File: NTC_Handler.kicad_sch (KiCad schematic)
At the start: 16 parts, among them U2 LM1117GS-3.3, U3 LMV331, U5 ADuM1200AR

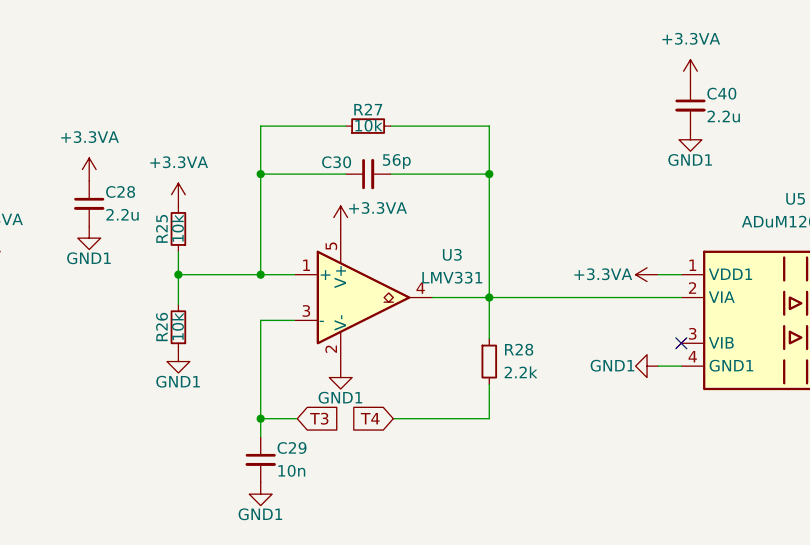
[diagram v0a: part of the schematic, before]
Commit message: Поменял компаратор на пушпульный
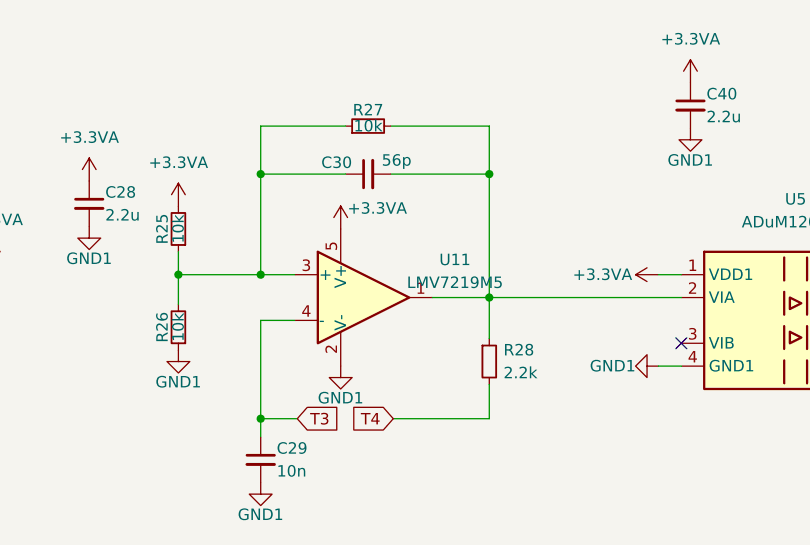
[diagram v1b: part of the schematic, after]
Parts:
- removed U3: LMV331, Package_TO_SOT_SMD:SOT-23-5, symbol Comparator:LMV331
- added U11: LMV7219M5, Package_TO_SOT_SMD:SOT-23-5, symbol Comparator:LMV7219M5
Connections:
- net +3.3VA: now also U11.5 (V+)
- net GND1: now also U11.2 (V-)
- net T3: now also U11.4 (-)
- net at C30.1, R25.1, R26.2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: now also U11.3 (+)
- net at C30.2, R27.2, R28.1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: now also U11.1

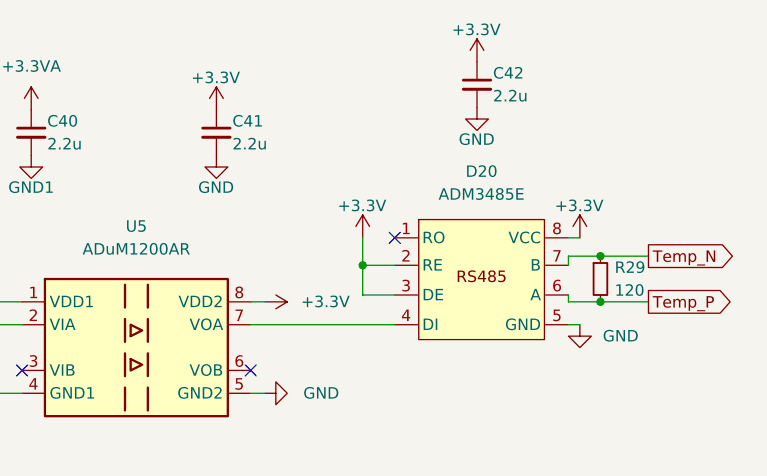
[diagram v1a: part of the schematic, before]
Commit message: Изменил схему
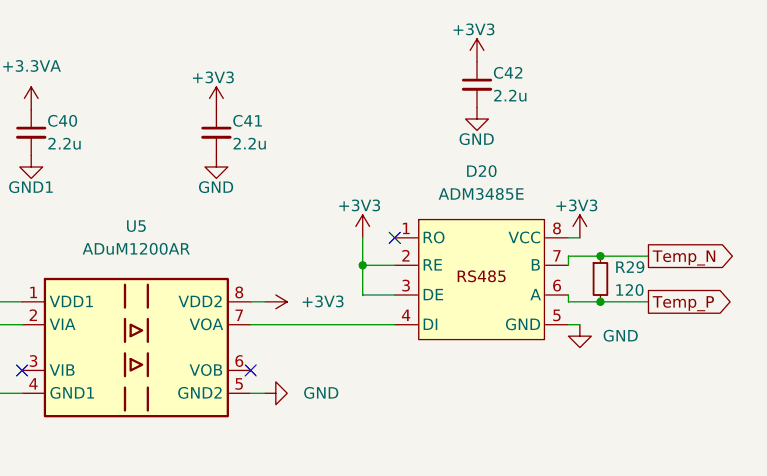
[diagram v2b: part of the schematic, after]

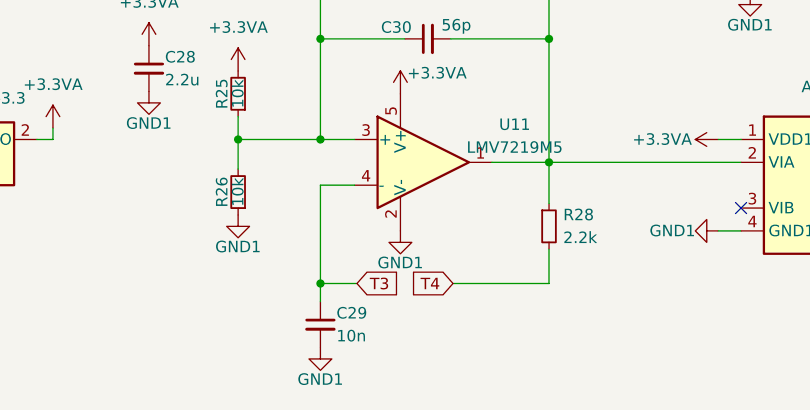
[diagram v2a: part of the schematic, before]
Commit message: Добавил температурные контуры звщиты
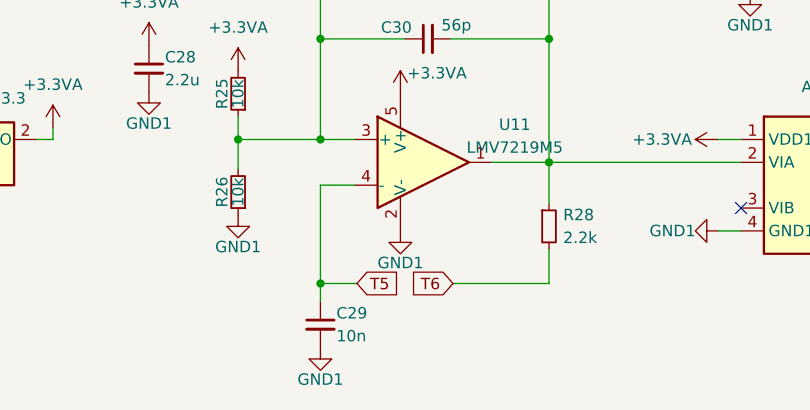
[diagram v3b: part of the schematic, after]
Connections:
- net T3 renamed T5
- net T4 renamed T6
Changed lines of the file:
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@@
 		)
 	)
-	(global_label "T4"
+	(global_label "T6"
 		(shape input)
 		(at 153.416 110.998 180)
@@
 		)
 		(property "Intersheetrefs" "${INTERSHEET_REFS}"
-			(at 148.8258 110.9186 0)
+			(at 148.7462 110.998 0)
 			(effects
 				(font
@@
 		)
 	)
-	(global_label "T3"
+	(global_label "T5"
 		(shape input)
 		(at 142.748 110.998 0)
@@
 		)
 		(property "Intersheetrefs" "${INTERSHEET_REFS}"
-			(at 147.3382 111.0774 0)
+			(at 147.4178 110.998 0)
 			(effects
 				(font

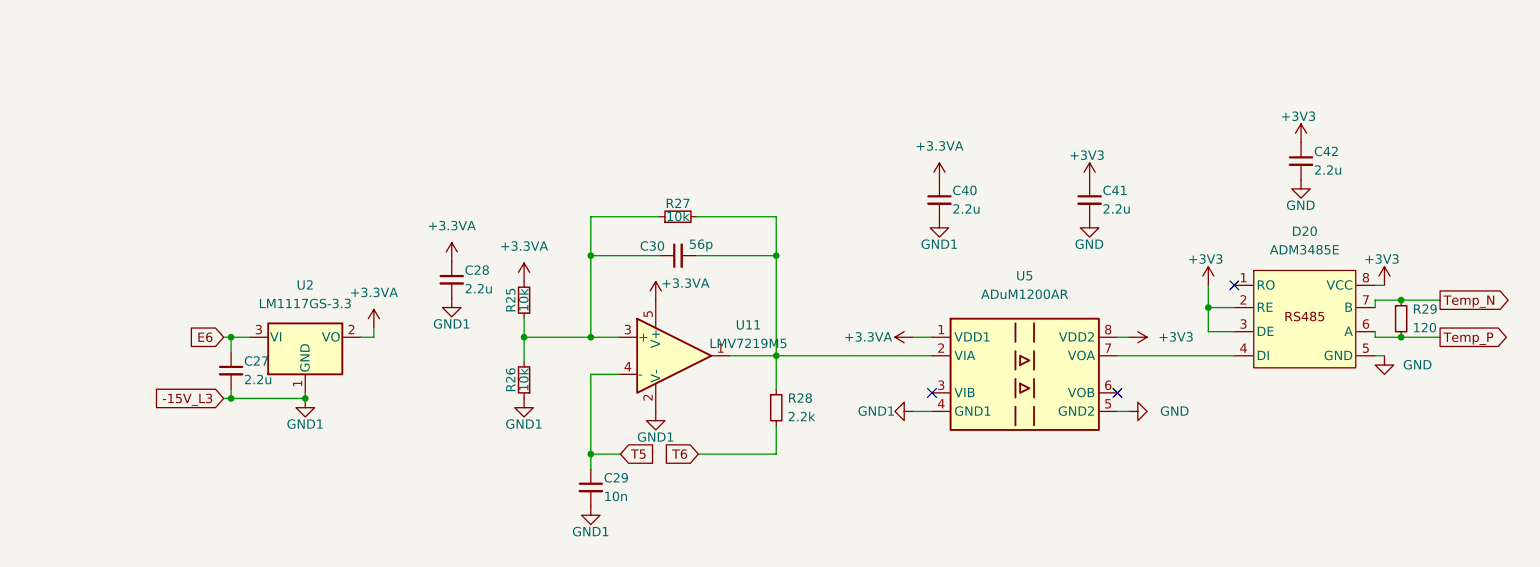
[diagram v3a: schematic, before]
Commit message: Убрал питание 3.3В
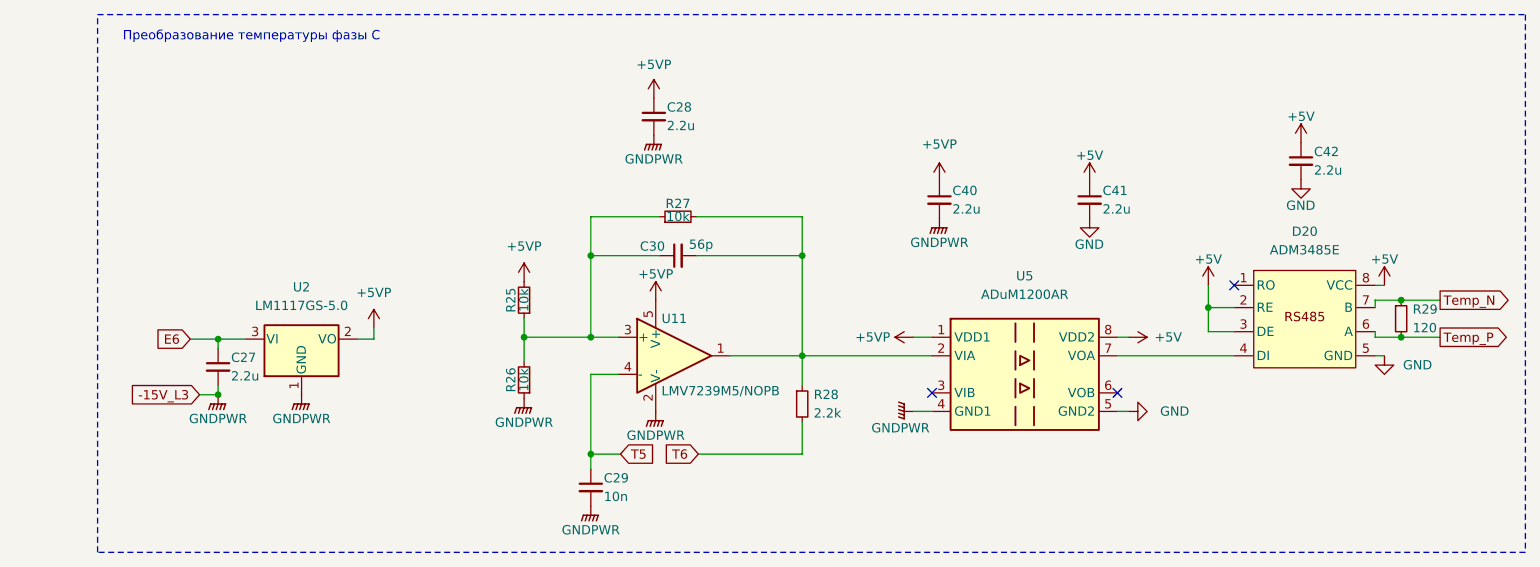
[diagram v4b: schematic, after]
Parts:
- U11: value LMV7219M5 -> LMV7239M5/NOPB
- U2: value LM1117GS-3.3 -> LM1117GS-5.0
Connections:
- net +3.3VA renamed +5VP
- net +3V3 renamed +5V
- net GND1 renamed GNDPWR
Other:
- note added: "Преобразование температуры фазы С"
- moved on the sheet: C27, C28, R28, U2

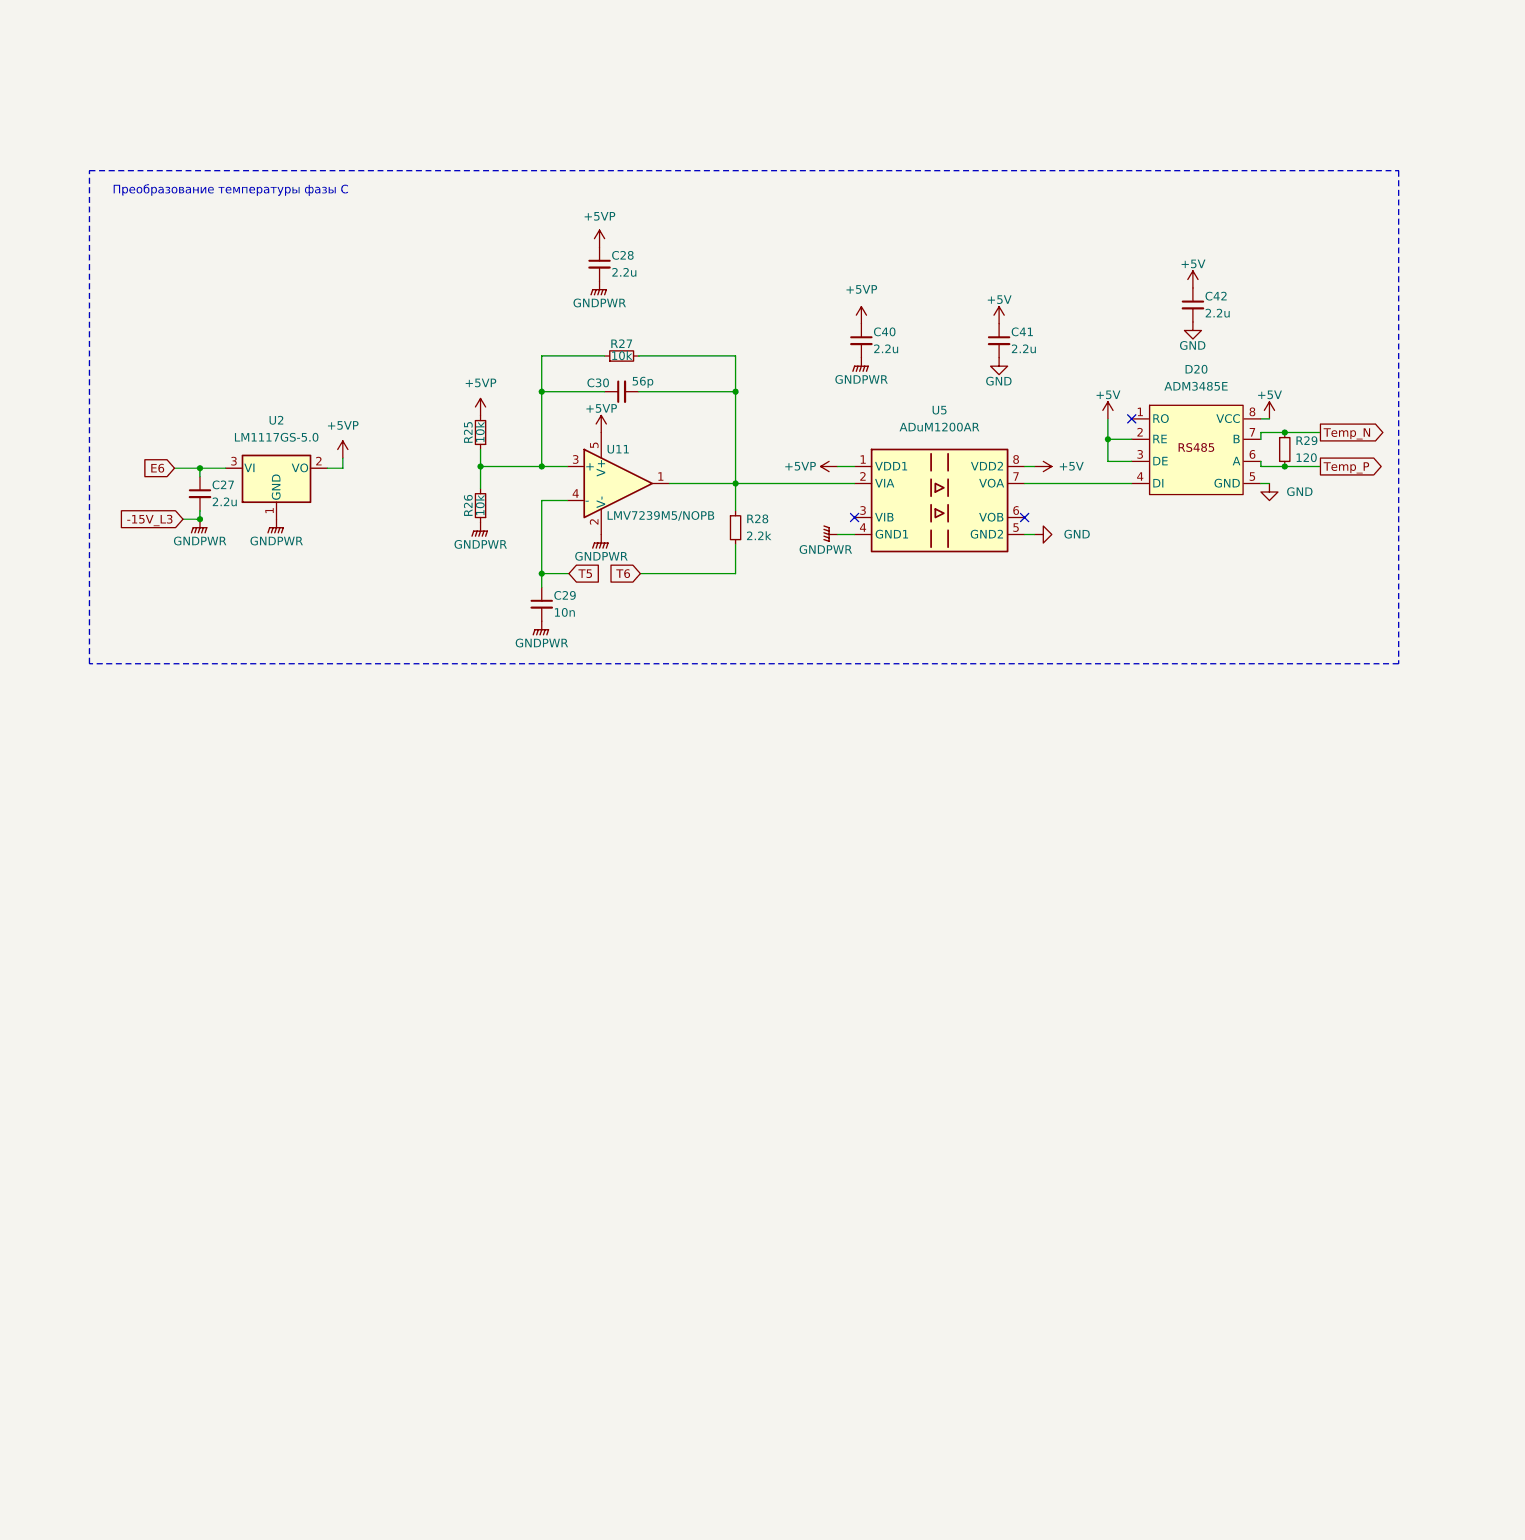
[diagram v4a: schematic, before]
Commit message: Развел стойку фазы А
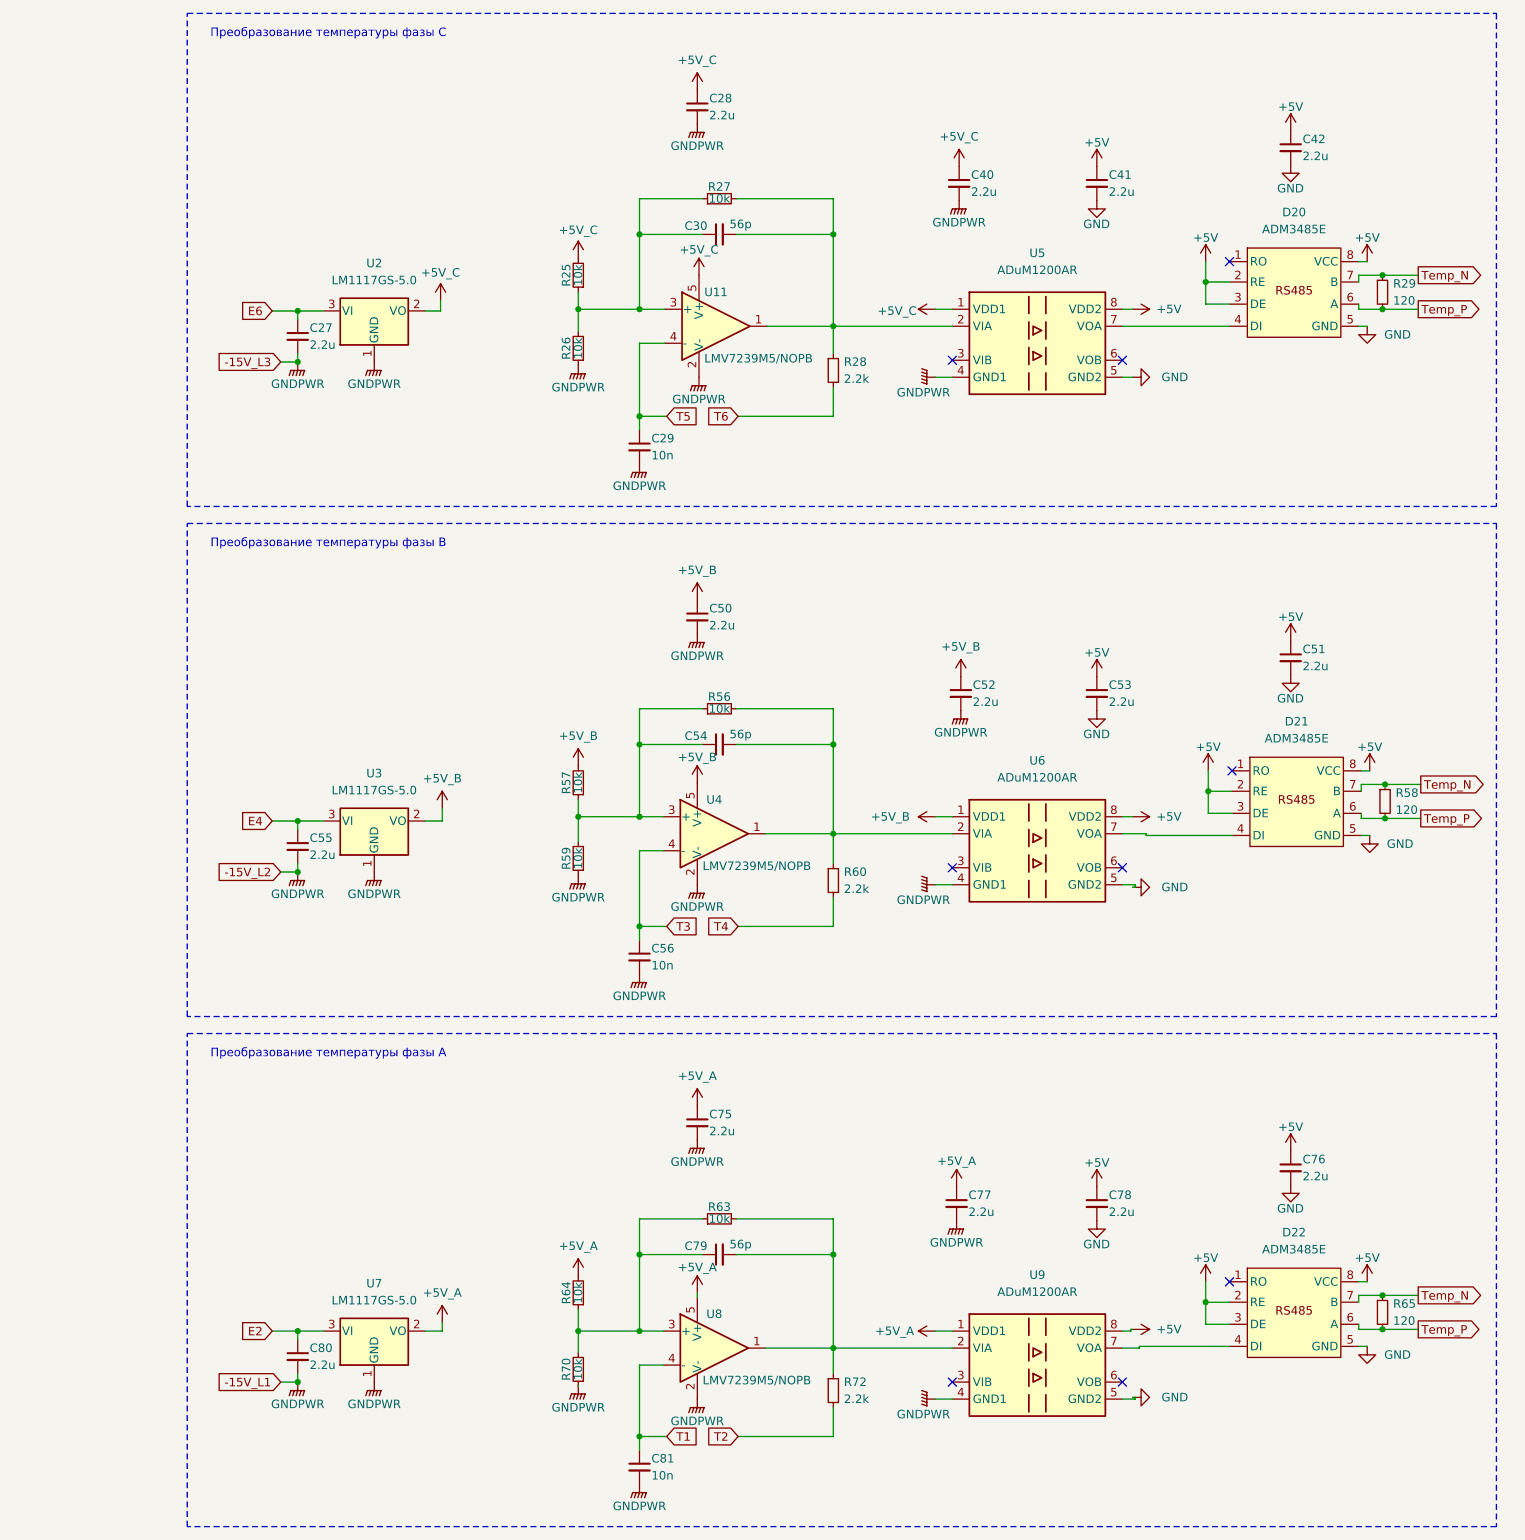
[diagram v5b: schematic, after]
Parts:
- added C50, C51, C52, C53, C55, C75, C76, C77, C78, C80: 2.2u, Capacitor_SMD:C_0805_2012Metric_Pad1.18x1.45mm_HandSolder, symbol Device:C_Small
- added C54, C79: 56p, Capacitor_SMD:C_0805_2012Metric_Pad1.18x1.45mm_HandSolder, symbol Device:C_Small
- added C56, C81: 10n, Capacitor_SMD:C_0805_2012Metric_Pad1.18x1.45mm_HandSolder, symbol Device:C_Small
- added D21, D22: ADM3485E, Package_SO:SOIC-8_3.9x4.9mm_P1.27mm, symbol Interface_My:ADM3485E
- added R56, R57, R59, R63, R64, R70: 10k, Resistor_SMD:R_0805_2012Metric_Pad1.20x1.40mm_HandSolder, symbol Device:R_Small
- added R58, R65: 120, Resistor_SMD:R_0805_2012Metric_Pad1.20x1.40mm_HandSolder, symbol Device:R_Small
- added R60, R72: 2.2k, Resistor_SMD:R_0805_2012Metric_Pad1.20x1.40mm_HandSolder, symbol Device:R_Small
- added U3, U7: LM1117GS-5.0, Package_TO_SOT_SMD:SOT-223, symbol Regulator_Linear:LM1117-3.3
- added U4, U8: LMV7239M5/NOPB, Package_TO_SOT_SMD:SOT-23-5, symbol Comparator:LMV7219M5
- added U6, U9: ADuM1200AR, Package_SO:SOIC-8_3.9x4.9mm_P1.27mm, symbol Isolator:ADuM1200AR
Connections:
- net +5V: now also C51.1, C53.1, C76.1, C78.1, D21.2 (RE), D21.3 (DE), D21.8 (VCC), D22.2 (RE), D22.3 (DE), D22.8 (VCC), U6.8 (VDD2), U9.8 (VDD2)
- net GND: now also C51.2, C53.2, C76.2, C78.2, D21.5 (GND), D22.5 (GND), U6.5 (GND2), U9.5 (GND2)
- net GNDPWR: now also C50.2, C52.2, C55.2, C56.2, C75.2, C77.2, C80.2, C81.2, R59.1, R70.1, U3.1 (GND), U4.2 (V-), U6.4 (GND1), U7.1 (GND), U8.2 (V-), U9.4 (GND1)
- net Temp_N: now also D21.7 (B), D22.7 (B), R58.1, R65.1
- net Temp_P: now also D21.6 (A), D22.6 (A), R58.2, R65.2
- net +5VP renamed +5V_C
- new net: C54.2, R56.2, R60.1, U4.1, U6.2 (VIA)
- new net: C54.1, R56.1, R57.1, R59.2, U4.3 (+)
- new net: D21.4 (DI), U6.7 (VOA)
- new net: C79.2, R63.2, R72.1, U8.1, U9.2 (VIA)
- new net: D22.4 (DI), U9.7 (VOA)
- new net: C79.1, R63.1, R64.1, R70.2, U8.3 (+)
- new net +5V_A: C75.1, C77.1, R64.2, U7.2 (VO), U8.5 (V+), U9.1 (VDD1)
- new net +5V_B: C50.1, C52.1, R57.2, U3.2 (VO), U4.5 (V+), U6.1 (VDD1)
- new net E2: C80.1, U7.3 (VI)
- new net E4: C55.1, U3.3 (VI)
- new net T1: C81.1, U8.4 (-)
- new net T2: R72.2
- new net T3: C56.1, U4.4 (-)
- new net T4: R60.2
- no-connect marks 3 -> 9
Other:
- note added: "Преобразование температуры фазы A"
- note added: "Преобразование температуры фазы B"
- moved on the sheet: C27, C28, C29, C30, C40, C41, C42, D20, R25, R26, R27, R28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
